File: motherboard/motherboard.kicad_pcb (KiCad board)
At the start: 2 copper layers, 85 x 56.5 mm, 29 parts, among them J1 Conn_01x02_Male, J2 Temp_connector, J3 24V_connector, P1 Raspberry_Pi_+_Conn, Q1 Q_NMOS_GSD, Q2 Q_NMOS_GSD, U1 74AUC2G04, U2 quad_and, U3 TLC272

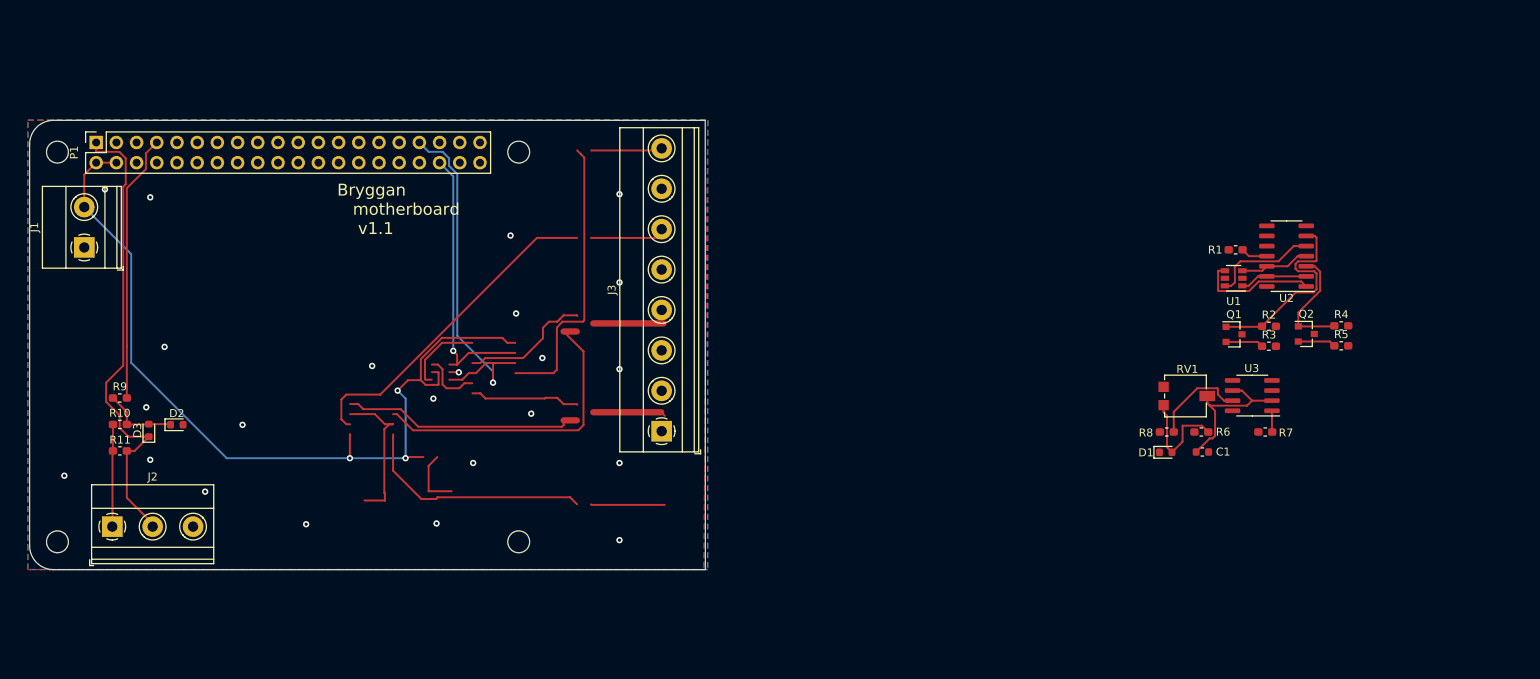
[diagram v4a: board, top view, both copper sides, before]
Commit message: Fixed edge cuts bug
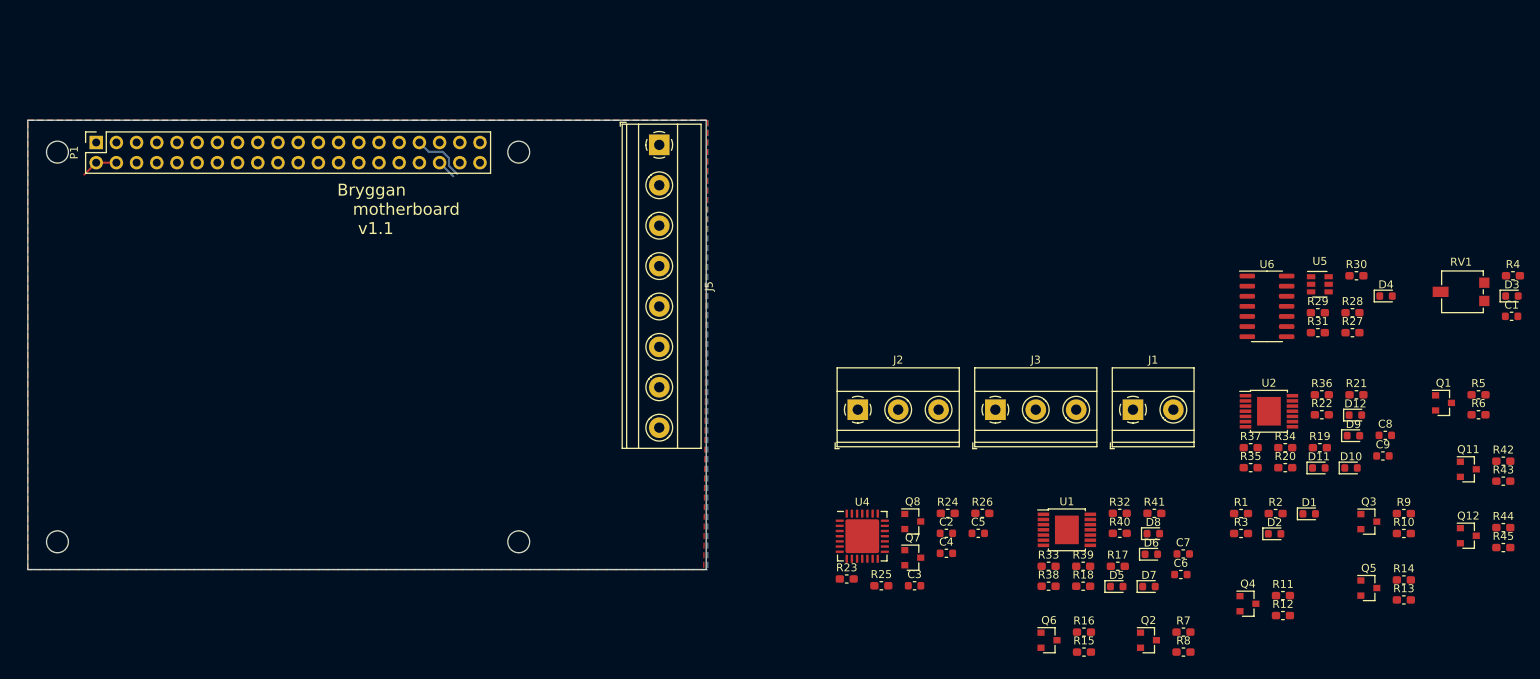
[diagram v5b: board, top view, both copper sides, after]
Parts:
- removed U3: TLC272, Package_SO:SOIC-8_3.9x4.9mm_P1.27mm
- added C2: 135pF, Capacitor_SMD:C_0603_1608Metric, F.Cu at (170.5, 90.4)
- added C3: 135pF, Capacitor_SMD:C_0603_1608Metric, F.Cu at (166.5, 97.0)
- added C4: 100nF, Capacitor_SMD:C_0603_1608Metric, F.Cu at (170.5, 93.0)
- added C5: 10pF, Capacitor_SMD:C_0603_1608Metric, F.Cu at (174.5, 90.4)
- added C6: 100nF, Capacitor_SMD:C_0603_1608Metric, F.Cu at (200.0, 95.6)
- added C7: 10pF, Capacitor_SMD:C_0603_1608Metric, F.Cu at (200.3, 93.0)
- added C8: 100nF, Capacitor_SMD:C_0603_1608Metric, F.Cu at (225.7, 78.1)
- added C9: 10pF, Capacitor_SMD:C_0603_1608Metric, F.Cu at (225.4, 80.7)
- added D10: LED, LED_SMD:LED_0603_1608Metric, F.Cu at (221.4, 82.2)
- added D11: LED, LED_SMD:LED_0603_1608Metric, F.Cu at (217.3, 82.2)
- added D12: LED, LED_SMD:LED_0603_1608Metric, F.Cu at (221.9, 75.6)
- added D4: LED, LED_SMD:LED_0603_1608Metric, F.Cu at (225.8, 60.6)
- added D5: LED, LED_SMD:LED_0603_1608Metric, F.Cu at (191.9, 97.1)
- added D6: LED, LED_SMD:LED_0603_1608Metric, F.Cu at (196.3, 93.1)
- added D7: LED, LED_SMD:LED_0603_1608Metric, F.Cu at (196.0, 97.1)
- added D8: LED, LED_SMD:LED_0603_1608Metric, F.Cu at (196.5, 90.5)
- added D9: LED, LED_SMD:LED_0603_1608Metric, F.Cu at (221.7, 78.2)
- added J5: 24VDC_connector, TerminalBlock_Phoenix:TerminalBlock_Phoenix_MKDS-1,5-8-5.08_1x08_P5.08mm_Horizontal, F.Cu at (134.4, 41.6)
- added Q11: Q_NMOS_GSD, Package_TO_SOT_SMD:SOT-23, F.Cu at (236.1, 82.4)
- added Q12: Q_NMOS_GSD, Package_TO_SOT_SMD:SOT-23, F.Cu at (236.1, 90.7)
- added Q3: Q_NMOS_GSD, Package_TO_SOT_SMD:SOT-23, F.Cu at (223.6, 89.0)
- added Q4: Q_NMOS_GSD, Package_TO_SOT_SMD:SOT-23, F.Cu at (208.4, 99.3)
- added Q5: Q_NMOS_GSD, Package_TO_SOT_SMD:SOT-23, F.Cu at (223.6, 97.3)
- added Q6: Q_NMOS_GSD, Package_TO_SOT_SMD:SOT-23, F.Cu at (183.4, 103.9)
- added Q7: Q_NMOS_GSD, Package_TO_SOT_SMD:SOT-23, F.Cu at (166.3, 93.5)
- added Q8: Q_NMOS_GSD, Package_TO_SOT_SMD:SOT-23, F.Cu at (166.3, 89.0)
- added R12: 5, Resistor_SMD:R_0603_1608Metric_Pad1.05x0.95mm_HandSolder, F.Cu at (212.8, 100.8)
- added R13: 100k, Resistor_SMD:R_0603_1608Metric_Pad1.05x0.95mm_HandSolder, F.Cu at (228.0, 98.8)
- added R14: 5, Resistor_SMD:R_0603_1608Metric_Pad1.05x0.95mm_HandSolder, F.Cu at (228.0, 96.3)
- added R15: 100k, Resistor_SMD:R_0603_1608Metric_Pad1.05x0.95mm_HandSolder, F.Cu at (187.8, 105.4)
- added R16: 5, Resistor_SMD:R_0603_1608Metric_Pad1.05x0.95mm_HandSolder, F.Cu at (187.8, 102.9)
- added R17: 4k7, Resistor_SMD:R_0603_1608Metric_Pad1.05x0.95mm_HandSolder, F.Cu at (192.1, 94.6)
- added R18: 4k7, Resistor_SMD:R_0603_1608Metric_Pad1.05x0.95mm_HandSolder, F.Cu at (187.7, 97.1)
- added R19: 4k7, Resistor_SMD:R_0603_1608Metric_Pad1.05x0.95mm_HandSolder, F.Cu at (217.5, 79.7)
- added R20: 240, Resistor_SMD:R_0603_1608Metric_Pad1.05x0.95mm_HandSolder, F.Cu at (213.1, 82.2)
- added R21: 4k7, Resistor_SMD:R_0603_1608Metric_Pad1.05x0.95mm_HandSolder, F.Cu at (222.1, 73.0)
- added R22: 240, Resistor_SMD:R_0603_1608Metric_Pad1.05x0.95mm_HandSolder, F.Cu at (217.7, 75.5)
- added R23: 10k, Resistor_SMD:R_0603_1608Metric_Pad1.05x0.95mm_HandSolder, F.Cu at (158.0, 96.2)
- added R24: 10k, Resistor_SMD:R_0603_1608Metric_Pad1.05x0.95mm_HandSolder, F.Cu at (170.7, 87.9)
- added R25: 1k, Resistor_SMD:R_0603_1608Metric_Pad1.05x0.95mm_HandSolder, F.Cu at (162.3, 97.0)
- added R26: 1k, Resistor_SMD:R_0603_1608Metric_Pad1.05x0.95mm_HandSolder, F.Cu at (175.0, 87.9)
- added R27: 100k, Resistor_SMD:R_0603_1608Metric_Pad1.05x0.95mm_HandSolder, F.Cu at (221.6, 65.2)
- added R28: 100k, Resistor_SMD:R_0603_1608Metric_Pad1.05x0.95mm_HandSolder, F.Cu at (221.6, 62.7)
- added R29: 3k3, Resistor_SMD:R_0603_1608Metric_Pad1.05x0.95mm_HandSolder, F.Cu at (217.2, 62.7)
- added R30: 5k6, Resistor_SMD:R_0603_1608Metric_Pad1.05x0.95mm_HandSolder, F.Cu at (222.1, 58.1)
- added R31: 240, Resistor_SMD:R_0603_1608Metric_Pad1.05x0.95mm_HandSolder, F.Cu at (217.2, 65.2)
- added R32: 4k7, Resistor_SMD:R_0603_1608Metric_Pad1.05x0.95mm_HandSolder, F.Cu at (192.3, 87.9)
- added R33: 4k7, Resistor_SMD:R_0603_1608Metric_Pad1.05x0.95mm_HandSolder, F.Cu at (183.4, 94.6)
- added R34: 4k7, Resistor_SMD:R_0603_1608Metric_Pad1.05x0.95mm_HandSolder, F.Cu at (213.1, 79.7)
- added R35: 240, Resistor_SMD:R_0603_1608Metric_Pad1.05x0.95mm_HandSolder, F.Cu at (208.8, 82.2)
- added R36: 4k7, Resistor_SMD:R_0603_1608Metric_Pad1.05x0.95mm_HandSolder, F.Cu at (217.7, 73.0)
- added R37: 240, Resistor_SMD:R_0603_1608Metric_Pad1.05x0.95mm_HandSolder, F.Cu at (208.8, 79.7)
- added R38: 240, Resistor_SMD:R_0603_1608Metric_Pad1.05x0.95mm_HandSolder, F.Cu at (183.4, 97.1)
- added R39: 240, Resistor_SMD:R_0603_1608Metric_Pad1.05x0.95mm_HandSolder, F.Cu at (187.7, 94.6)
- added R40: 240, Resistor_SMD:R_0603_1608Metric_Pad1.05x0.95mm_HandSolder, F.Cu at (192.3, 90.4)
- added R41: 240, Resistor_SMD:R_0603_1608Metric_Pad1.05x0.95mm_HandSolder, F.Cu at (196.7, 87.9)
- added R42: 100k, Resistor_SMD:R_0603_1608Metric_Pad1.05x0.95mm_HandSolder, F.Cu at (240.5, 81.4)
- added R43: 5, Resistor_SMD:R_0603_1608Metric_Pad1.05x0.95mm_HandSolder, F.Cu at (240.5, 83.9)
- added R44: 100k, Resistor_SMD:R_0603_1608Metric_Pad1.05x0.95mm_HandSolder, F.Cu at (240.5, 89.7)
- added R45: 5, Resistor_SMD:R_0603_1608Metric_Pad1.05x0.95mm_HandSolder, F.Cu at (240.5, 92.2)
- added U4: MCP23017_ML, Package_DFN_QFN:QFN-28-1EP_6x6mm_P0.65mm_EP4.25x4.25mm, F.Cu at (159.9, 90.8)
- added U5: 74AUC2G04, Package_TO_SOT_SMD:SOT-23-6, F.Cu at (217.5, 59.1)
- added U6: quad_and, Package_SO:SOIC-14_3.9x8.7mm_P1.27mm, F.Cu at (210.8, 61.9)
- D1: value d -> D
- D3: value D -> d
- J1: value Conn_01x02_Male -> power_conn
- J2: value Temp_connector -> serial_comm_conn
- J3: value 24V_connector -> Temp_connector; footprint TerminalBlock_Phoenix:TerminalBlock_Phoenix_MKDS-1,5-8-5.08_1x08_P5.08mm_Horizontal -> TerminalBlock_Phoenix:TerminalBlock_Phoenix_MKDS-1,5-3-5.08_1x03_P5.08mm_Horizontal
- R1: value R -> 100
- R10: value 100 -> 5
- R11: value 4.7k -> 100k
- R2: value 100k -> 100
- R3: value 30 -> 4.7k
- R4: value 100k -> 230
- R5: value 30 -> 100k
- R6, R8: value 230 -> 5
- R7: value 230 -> 100k
- R9: value 100 -> 100k
- U1: value 74AUC2G04 -> LM324; footprint Package_TO_SOT_SMD:SOT-23-6 -> Package_SO:TSSOP-14-1EP_4.4x5mm_P0.65mm
- U2: value quad_and -> LM324; footprint Package_SO:SOIC-14_3.9x8.7mm_P1.27mm -> Package_SO:TSSOP-14-1EP_4.4x5mm_P0.65mm
- moved D3 172.2 mm to (241.6, 60.6), turned to 0 degrees
- moved R9 162.1 mm to (228.0, 88.0)
- moved R10 162.0 mm to (228.0, 90.5)
- moved R11 147.4 mm to (212.8, 98.3), turned to 0 degrees
- moved D2 138.7 mm to (211.8, 90.5)
- moved J1 133.4 mm to (194.0, 74.9), turned to 0 degrees
- moved J2 94.9 mm to (159.4, 74.9)
- moved Q2 43.3 mm to (195.9, 103.9)
- moved C1 42.5 mm to (241.6, 63.2)
- moved J3 42.1 mm to (176.7, 74.9), turned to 0 degrees
- moved U1 37.9 mm to (185.7, 90.0), turned to 0 degrees
- moved RV1 37.2 mm to (235.4, 60.1), turned to 0 degrees
- moved R6 34.9 mm to (237.4, 75.5)
- moved R1 33.2 mm to (207.6, 88.0)
- moved R8 27.7 mm to (200.3, 105.4), turned to 0 degrees
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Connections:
- net Net-(P1-Pad10) renamed /VFD_comm/rxd_pi
- net Net-(P1-Pad8) renamed /VFD_comm/txd_pi
- C1 pad 1: Net-(C1-Pad1) -> /low_side_outputs/SSR_1_2_comparator/reference_voltage
- D1 pad 1: GND -> Net-(D1-Pad1)
- D1 pad 2: Net-(D1-Pad2) -> GND
- D2 pad 1: Net-(D2-Pad1) -> /TEMP_IN_PWR
- D2 pad 2: GND -> Net-(D1-Pad1)
- D3 pad 1: /TEMP_IN_PWR -> GND
- D3 pad 2: Net-(D2-Pad1) -> Net-(D3-Pad2)
- J2 pad 1: /TEMP_IN_MEAS -> /VFD_comm/txd_conn
- J2 pad 2: /TEMP_IN_PWR -> /VFD_comm/rxd_conn
- J3 pad 1: /SSR_in_1_enc -> /TEMP_IN_MEAS
- J3 pad 2: /SSR_in_2_enc -> /TEMP_IN_PWR
- J3 pad 3: /220V_1 -> GND
- P1 pad 14: Net-(P1-Pad14) -> GND
- P1 pad 18: Net-(P1-Pad18) -> /SSR_interface/error_signal
- P1 pad 25: Net-(P1-Pad25) -> GND
- P1 pad 3: Net-(P1-Pad3) -> /i2c_interface/sda
- P1 pad 30: Net-(P1-Pad30) -> GND
- P1 pad 33: /SSR_interface/SSR2_GPIO -> Net-(P1-Pad33)
- P1 pad 34: Net-(P1-Pad34) -> GND
- P1 pad 36: /SSR_interface/SSR1_GPIO -> Net-(P1-Pad36)
- P1 pad 39: Net-(P1-Pad39) -> GND
- P1 pad 5: Net-(P1-Pad5) -> /i2c_interface/sck
- P1 pad 6: Net-(P1-Pad6) -> GND
- P1 pad 7: /Temp_interface/TEMP_GPIO -> /temp_interface/TEMP_GPIO
- P1 pad 9: Net-(P1-Pad9) -> GND
- Q1 pad 1: /SSR_interface/SSR_driver_1/sig_in -> /SSR_interface/SSR2_GPIO_safe
- Q1 pad 2: /SSR_interface/SSR_driver_1/indicator -> /low_side_outputs/SSR2_driver/indicator
- Q1 pad 3: /SSR_in_1_enc -> /SSR_2_enclosure
- Q2 pad 1: /SSR_interface/SSR_driver_2/sig_in -> /i2c_interface/relay_1_i2c_out
- Q2 pad 2: /SSR_interface/SSR_driver_2/indicator -> /low_side_outputs/relay_1_driver/indicator
- Q2 pad 3: /SSR_in_2_enc -> /relay_1_enclosure
- R1 pad 1: /SSR_interface/error_signal -> Net-(D1-Pad1)
- R1 pad 2: Net-(R1-Pad2) -> /temp_interface/TEMP_GPIO
- R10 pad 1: /TEMP_IN_MEAS -> /low_side_outputs/relay_2_driver/indicator
- R10 pad 2: Net-(D2-Pad1) -> GND
- R11 pad 1: /TEMP_IN_PWR -> /i2c_interface/relay_3_i2c_out
- R11 pad 2: /TEMP_IN_MEAS -> GND
- R2 pad 1: /SSR_interface/SSR_driver_1/sig_in -> /TEMP_IN_MEAS
- R2 pad 2: GND -> Net-(D1-Pad1)
- R3 pad 1: /SSR_interface/SSR_driver_1/indicator -> /TEMP_IN_PWR
- R3 pad 2: GND -> /TEMP_IN_MEAS
- R4 pad 1: /SSR_interface/SSR_driver_2/sig_in -> +5V
- R4 pad 2: GND -> Net-(D3-Pad2)
- R5 pad 1: /SSR_interface/SSR_driver_2/indicator -> /SSR_interface/SSR2_GPIO_safe
- R6 pad 1: +5V -> /low_side_outputs/SSR2_driver/indicator
- R6 pad 2: Net-(D1-Pad2) -> GND
- R7 pad 1: Net-(R7-Pad1) -> /i2c_interface/relay_1_i2c_out
- R7 pad 2: /SSR_interface/indicator_1_pi -> GND
- R8 pad 1: Net-(R8-Pad1) -> /low_side_outputs/relay_1_driver/indicator
- R8 pad 2: /SSR_interface/indicator_2_pi -> GND
- R9 pad 1: Net-(D2-Pad1) -> /i2c_interface/relay_2_i2c_out
- R9 pad 2: /Temp_interface/TEMP_GPIO -> GND
- RV1 pad 1: Net-(D1-Pad2) -> Net-(D3-Pad2)
- RV1 pad 2: Net-(C1-Pad1) -> /low_side_outputs/SSR_1_2_comparator/reference_voltage
- U1 pad 1: /SSR_interface/SSR1_GPIO -> Net-(R17-Pad1)
- U1 pad 2: GND -> /low_side_outputs/SSR_1_2_comparator/reference_voltage
- U1 pad 3: /SSR_interface/SSR2_GPIO -> /low_side_outputs/SSR1_driver/indicator
- U1 pad 4: Net-(U1-Pad4) -> +5V
- U1 pad 5: +5V -> /low_side_outputs/SSR2_driver/indicator
- U1 pad 6: Net-(U1-Pad6) -> /low_side_outputs/SSR_1_2_comparator/reference_voltage
- U2 pad 1: Net-(U1-Pad4) -> Net-(R19-Pad1)
- U2 pad 10: Net-(U2-Pad10) -> /low_side_outputs/relay_3_driver/indicator
- U2 pad 11: Net-(R1-Pad2) -> GND
- U2 pad 12: /SSR_interface/SSR2_GPIO -> /low_side_outputs/relay_4_driver/indicator
- U2 pad 13: /SSR_interface/SSR1_GPIO -> /low_side_outputs/SSR_1_2_comparator/reference_voltage
- U2 pad 14: +5V -> Net-(R36-Pad1)
- U2 pad 2: /SSR_interface/SSR1_GPIO -> /low_side_outputs/SSR_1_2_comparator/reference_voltage
- U2 pad 3: /SSR_interface/SSR_driver_2/sig_in -> /low_side_outputs/relay_1_driver/indicator
- U2 pad 4: /SSR_interface/SSR2_GPIO -> +5V
- U2 pad 5: Net-(U1-Pad6) -> /low_side_outputs/relay_2_driver/indicator
- U2 pad 6: /SSR_interface/SSR_driver_1/sig_in -> /low_side_outputs/SSR_1_2_comparator/reference_voltage
- U2 pad 7: GND -> Net-(R21-Pad1)
- U2 pad 9: Net-(U2-Pad9) -> /low_side_outputs/SSR_1_2_comparator/reference_voltage
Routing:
- net /5V+: track 108.7 -> 4.66 mm, vias 3 -> 0
- net Net-(R8-Pad1): track 93.7 -> 0.00 mm
- net /TEMP_IN_PWR: track 59.0 -> 0.00 mm
- net Net-(C1-Pad1): track 57.4 -> 0.00 mm
- net /SSR_interface/SSR2_GPIO: track 55.5 -> 0.00 mm, vias 1 -> 0
- net /SSR_interface/SSR1_GPIO: track 43.7 -> 0.00 mm, vias 1 -> 0
- net /SSR_interface/SSR_driver_1/sig_in: track 39.7 -> 0.00 mm
- net Net-(R1-Pad2): track 39.7 -> 0.00 mm
- net /SSR_interface/SSR_driver_1/indicator: track 35.2 -> 0.00 mm
- net /Temp_interface/TEMP_GPIO: track 33.7 -> 0.00 mm
- net Net-(D1-Pad2): track 32.7 -> 0.00 mm
- net /SSR_interface/SSR_driver_2/sig_in: track 31.1 -> 0.00 mm
- net Net-(U1-Pad6): track 23.6 -> 0.00 mm
- net Net-(U1-Pad4): track 22.9 -> 0.00 mm
- net /TEMP_IN_MEAS: track 12.5 -> 0.00 mm
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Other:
- board size 85 x 56.5 mm -> 85.3 x 56.5 mm

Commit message: i2c subcircuit routed
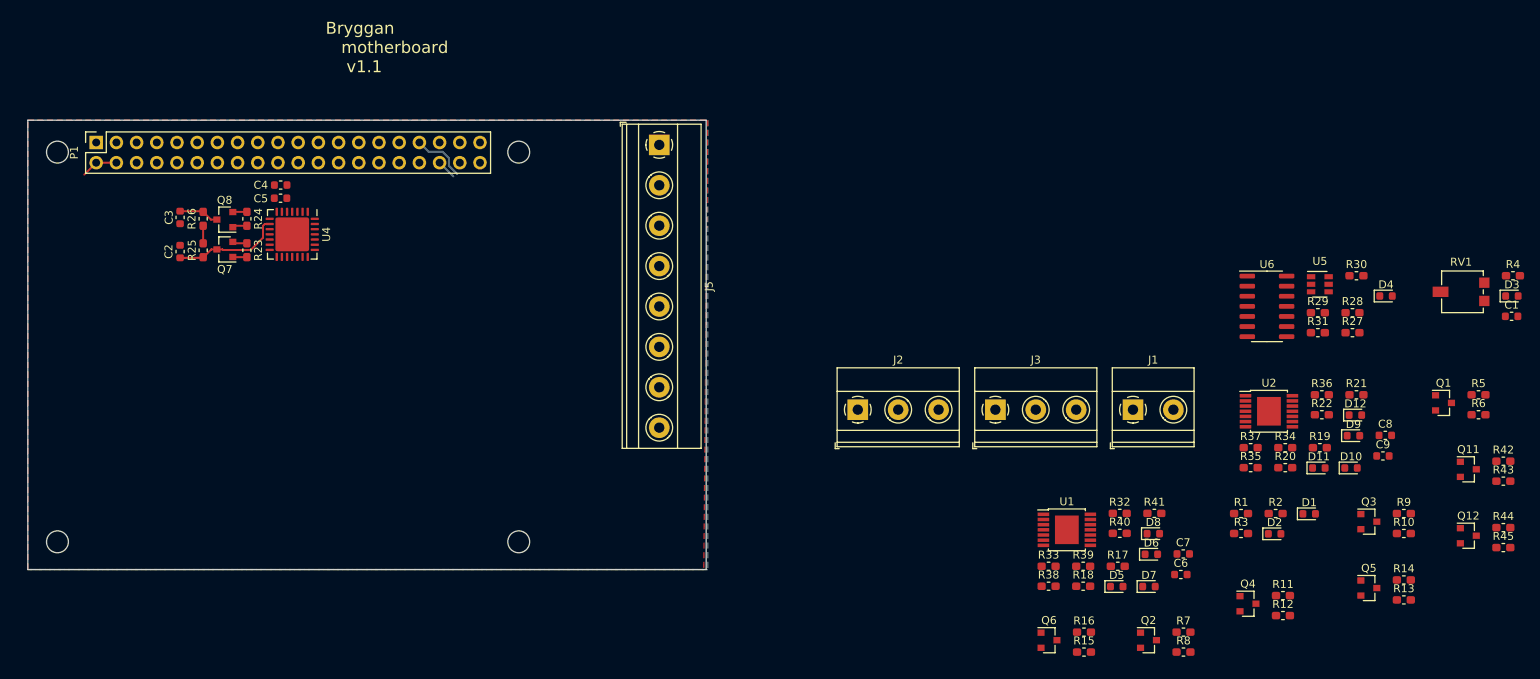
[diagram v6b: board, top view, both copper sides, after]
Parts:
- moved R26 104.7 mm to (77.0, 50.9), turned to 90 degrees
- moved C3 103.3 mm to (74.2, 50.7), turned to 270 degrees
- moved C2 102.7 mm to (74.2, 55.0), turned to 90 degrees
- moved C5 97.3 mm to (86.8, 48.3), turned to 180 degrees
- moved C4 95.7 mm to (86.8, 46.6), turned to 180 degrees
- moved R24 95.6 mm to (82.5, 50.9), turned to 270 degrees
- moved R25 95.1 mm to (77.0, 54.9), turned to 270 degrees
- moved Q7 94.8 mm to (79.8, 54.7), turned to 180 degrees
- moved Q8 94.5 mm to (79.8, 51.0), turned to 180 degrees
- moved R23 86.0 mm to (82.5, 54.8), turned to 270 degrees
- moved U4 81.1 mm to (88.2, 52.9), turned to 270 degrees
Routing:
- net Net-(C2-Pad1): track 0.00 -> 14.0 mm
- net Net-(C3-Pad1): track 0.00 -> 5.06 mm
- net +3V3: track 0.00 -> 3.90 mm
- net +5V: track 0.00 -> 2.21 mm
- net /i2c_interface/sda: track 0.00 -> 1.96 mm
- net /i2c_interface/sck: track 0.00 -> 1.83 mm

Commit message: Showcase PCB
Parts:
- added G***: LOGO, graphic:bryggans_logo, F.Cu at (72.1, 81.9)
- moved R4 159.1 mm to (82.7, 60.1), turned to 90 degrees
- moved D3 156.4 mm to (85.2, 60.2), turned to 90 degrees
- moved C1 153.8 mm to (87.8, 60.3), turned to 90 degrees
- moved RV1 150.9 mm to (84.7, 66.5), turned to 90 degrees
- moved J1 134.4 mm to (60.8, 57.0), turned to 90 degrees
- moved D1 128.3 mm to (87.9, 83.9), turned to 90 degrees
- moved R2 124.1 mm to (87.9, 88.1), turned to 90 degrees
- moved D2 121.4 mm to (90.4, 88.3), turned to 90 degrees
- moved R1 119.8 mm to (87.9, 92.5), turned to 90 degrees
- moved R45 118.5 mm to (122.9, 77.9), turned to 180 degrees
- moved R6 118.3 mm to (123.0, 45.5), turned to 180 degrees
- moved C9 118.3 mm to (107.1, 79.5)
- moved R35 118.3 mm to (90.5, 80.9)
- moved R37 118.3 mm to (90.5, 78.4)
- moved D11 118.3 mm to (99.1, 81.0)
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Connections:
- D2 pad 1: /TEMP_IN_PWR -> +3V3
- J1 pad 2: /5V+ -> +5V
- J3 pad 2: /TEMP_IN_PWR -> +3V3
- J5 pad 7: Net-(J5-Pad7) -> /extra_1_enclosure
- J5 pad 8: Net-(J5-Pad8) -> /extra_2_enclosure
- P1 pad 1: /TEMP_IN_PWR -> +3V3
- P1 pad 2: /5V+ -> +5V
- P1 pad 4: /5V+ -> +5V
- Q11 pad 3: /low_side_outputs/extra_1_driver/drain -> /extra_1_enclosure
- Q12 pad 3: /low_side_outputs/extra_2_driver/drain -> /extra_2_enclosure
- R3 pad 1: /TEMP_IN_PWR -> +3V3
- R32 pad 2: /low_side_outputs/extra_1_indicator -> /extra_1_ind
- R33 pad 2: /low_side_outputs/extra_2_indicator -> /extra_2_ind
- U4 pad 11: Net-(U4-Pad11) -> GND
- U4 pad 12: Net-(U4-Pad12) -> GND
- U4 pad 13: Net-(U4-Pad13) -> GND
- U4 pad 14: Net-(U4-Pad14) -> +5V
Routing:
- net Net-(P1-Pad33): track 6.95 -> 0.00 mm
- net /low_side_outputs/SSR1_driver/indicator: track 0.00 -> 6.03 mm
- net /SSR_interface/SSR1_GPIO_safe: track 0.00 -> 5.40 mm
- net /5V+: track 4.66 -> 0.00 mm
- net +5V: track 2.21 -> 6.87 mm
- net Net-(P1-Pad36): track 2.43 -> 0.00 mm

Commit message: Tried some placements
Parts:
- removed ? (x4): , RPi_Hat:RPi_Hat_Mounting_Hole
- removed G***: LOGO, graphic:bryggans_logo
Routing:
- net /low_side_outputs/SSR1_driver/indicator: track 6.03 -> 4.33 mm
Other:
- board text removed: "Bryggan motherboard v1.1"
